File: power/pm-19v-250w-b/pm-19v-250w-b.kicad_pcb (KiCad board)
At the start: 4 copper layers, 58.4 x 22.9 mm, 63 parts, among them J1 Screw pads S1-S4, J2 Aux header 2x3 1.27, Q1 BSC098N10NS5, Q2 BSC070N10NS5, Q3 BCX56-16, U1 LM5116MHX, U2 MCP65R46-2.4, U3 MCP65R46-2.4, U4 TPS3701DDCR

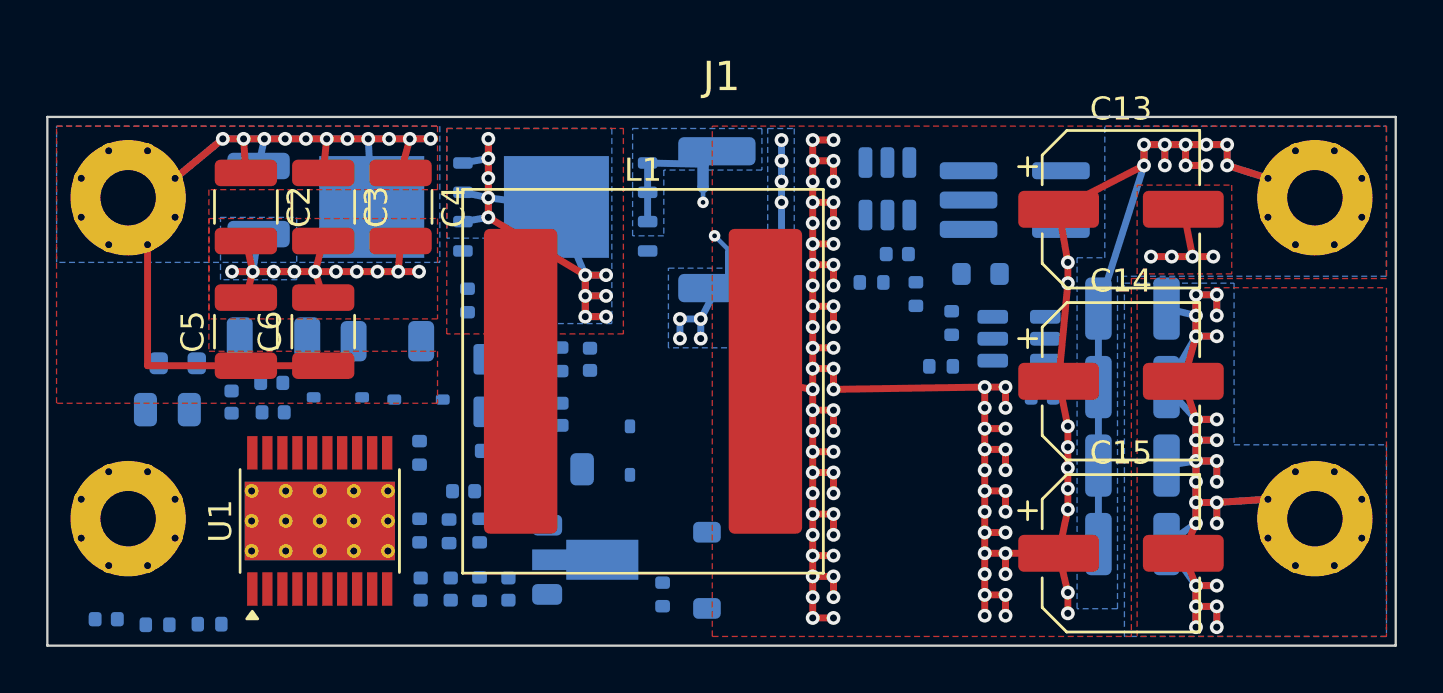
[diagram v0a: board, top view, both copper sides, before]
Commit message: PM-19V-250W-B board routed and fab-ready: U1 on F (pin order matches the power stage), its drive parts hand-placed on B, gate drive / bootstrap / VCC / VCCX / LO and the CS Kelvin taps as kept hand copper in tools/power.py, krt-route + two krt-reroute passes, GND pour (outer pours solid), pcbkit silk, prune; ERC 0, DRC 0 / 0 unconnected / parity clean (--refill-zones --severity-all), no In2 tracks; B heights inside the 7.0 mm gap; jlcfab: 38 lines, 60 parts, all JLC-stocked for 10 modules (2.31 / module), 12 per-LCSC CPL corrections (preview checklist in the spec, section 8: polymers C13-C15, Q3 bottom offset, Q1 / Q2, U1, J2, U2-U4, D1-D4)
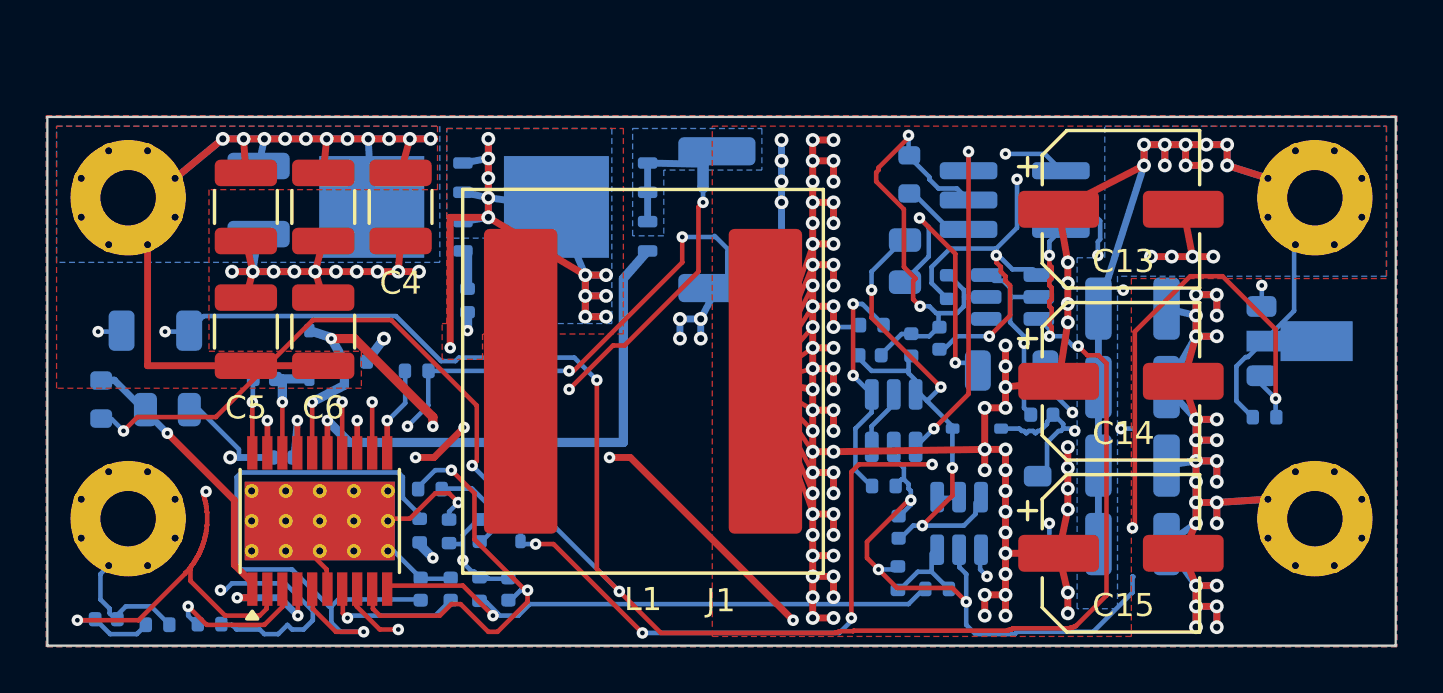
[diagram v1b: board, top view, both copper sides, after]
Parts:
- moved Q3 32.4 mm to (154.5, 109.7)
- moved R6 27.2 mm to (152.7, 113.0), turned to 0 degrees
- moved R15 27.1 mm to (141.8, 111.0)
- moved U4 22.4 mm to (141.8, 107.8), turned to 0 degrees
- moved C25 20.8 mm to (143.1, 112.9), turned to 0 degrees
- moved C24 20.0 mm to (138.6, 109.6), turned to 90 degrees
- moved R17 17.4 mm to (137.1, 106.2), turned to 90 degrees
- moved R16 17.0 mm to (139.0, 107.4)
- moved D4 15.1 mm to (140.3, 113.5), turned to 0 degrees
- moved D2 14.5 mm to (142.9, 117.2)
- moved C26 13.9 mm to (137.4, 109.9)
- moved R20 11.5 mm to (138.5, 120.4), turned to 0 degrees
- moved U2 10.0 mm to (136.7, 113.2)
- moved R21 9.36 mm to (136.8, 120.0), turned to 90 degrees
- moved R19 8.43 mm to (136.2, 116.0), turned to 0 degrees
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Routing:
- net /RUN: track 0.00 -> 103.8 mm, vias 0 -> 8
- net GND: track 124.3 -> 220.0 mm, vias 46 -> 60
- net /VOUT: track 160.4 -> 244.0 mm, vias 91 -> 87
- net /VIN: track 72.8 -> 143.5 mm, vias 11 -> 20
- net /VCCX: track 0.00 -> 60.0 mm, vias 0 -> 6
- net /VAUX: track 0.00 -> 38.6 mm, vias 0 -> 5
- net /OVS: track 0.00 -> 33.3 mm, vias 0 -> 4
- net /RAMP: track 0.00 -> 27.7 mm, vias 0 -> 1
- net /PGOOD: track 0.00 -> 26.3 mm, vias 0 -> 2
- net /VB: track 0.00 -> 26.3 mm, vias 0 -> 3
- net /LO: track 0.00 -> 23.3 mm, vias 0 -> 1
- net /CSG: track 0.99 -> 23.2 mm, vias 1 -> 4
- net /CS: track 0.65 -> 22.4 mm, vias 1 -> 3
- net /SW: track 30.2 -> 51.2 mm, vias 11 -> 13
- net /VCC: track 0.00 -> 19.7 mm, vias 0 -> 4
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- added copper zone on In2.Cu, net GND
